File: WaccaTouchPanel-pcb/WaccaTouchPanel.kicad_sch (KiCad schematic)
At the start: 106 parts, among them IC1 W25Q16JVUXIQ_TR, IC2 AT42QT2120-MMHR, IC3 AT42QT2120-MMHR, J1 USB_C_Receptacle_USB2.0, J10 SESNSOR2, J11 SESNSOR9, J12 SESNSOR1, J13 SESNSOR10, J14 SESNSOR11, J15 SESNSOR12, J16 SESNSOR19, J17 SESNSOR18, J18 SESNSOR17, J19 SESNSOR16, J2 RJ45_LED_Shielded, J20 SESNSOR15, J21 SESNSOR20, J22 SESNSOR14, J23 SESNSOR13, J24 Conn_02x06_Odd_Even, J25 Conn_02x06_Odd_Even, J26 Conn_02x06_Odd_Even, J27 Conn_02x06_Odd_Even, J28 Conn_02x06_Odd_Even, J3 SESNSOR7, J4 SESNSOR6, J5 Conn_01x03_Male, J6 SESNSOR5, J7 SESNSOR4, J8 SESNSOR3, J9 SESNSOR8, SW1 Program, SW3 Reset, U1 NCP1117-3.3_SOT223, U3 RP2040, Y1 ABLS-12.000MHZ-B4-T

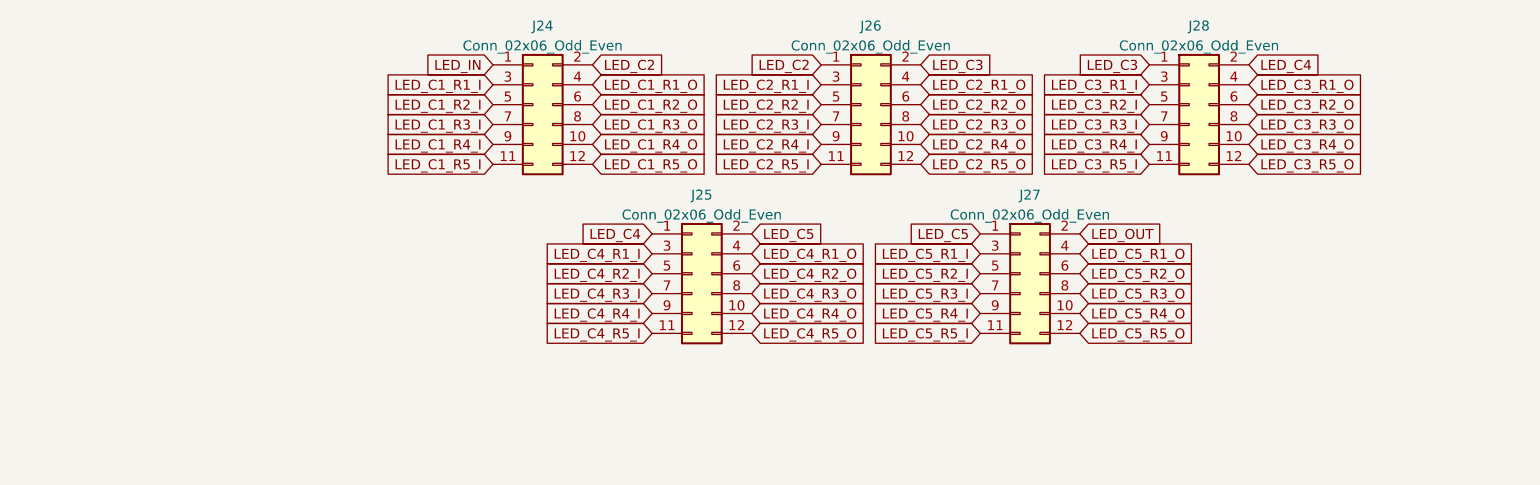
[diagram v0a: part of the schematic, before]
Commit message: finished Touch Panel PCB and added it to actions
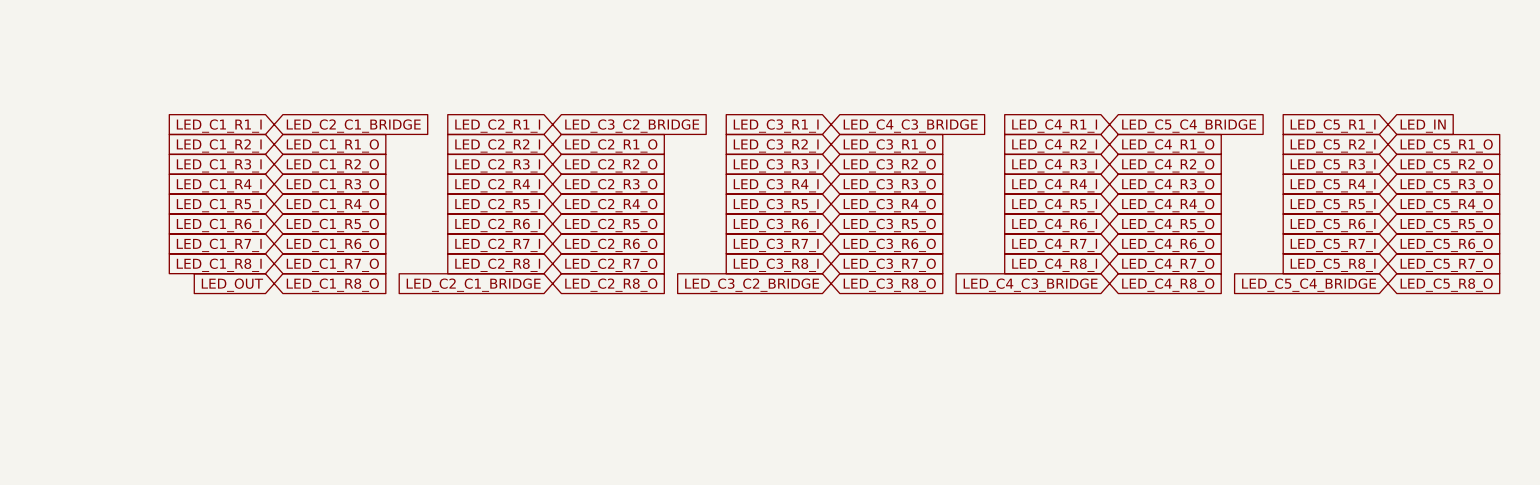
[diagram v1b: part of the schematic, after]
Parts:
- removed J24, J25, J26, J27, J28: Conn_02x06_Odd_Even, Connector_PinHeader_2.54mm:PinHeader_2x06_P2.54mm_Vertical, symbol Connector_Generic:Conn_02x06_Odd_Even
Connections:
- net LED_C1_R2_I is gone; now on net LED_C1_R1_O: D4.4 (DIN)
- net LED_C1_R3_I is gone; now on net LED_C1_R2_O: D5.4 (DIN)
- net LED_C1_R4_I is gone; now on net LED_C1_R3_O: D6.4 (DIN)
- net LED_C1_R5_I is gone; now on net LED_C1_R4_O: D7.4 (DIN)
- net LED_C1_R6_I is gone; now on net LED_C1_R5_O: D28.4 (DIN)
- net LED_C1_R7_I is gone; now on net LED_C1_R6_O: D29.4 (DIN)
- net LED_C1_R8_I is gone; now on net LED_C1_R7_O: D30.4 (DIN)
- net LED_C2_R2_I is gone; now on net LED_C2_R1_O: D9.4 (DIN)
- net LED_C2_R3_I is gone; now on net LED_C2_R2_O: D10.4 (DIN)
- net LED_C2_R4_I is gone; now on net LED_C2_R3_O: D11.4 (DIN)
- net LED_C2_R5_I is gone; now on net LED_C2_R4_O: D12.4 (DIN)
- net LED_C2_R6_I is gone; now on net LED_C2_R5_O: D31.4 (DIN)
- net LED_C2_R7_I is gone; now on net LED_C2_R6_O: D32.4 (DIN)
- net LED_C2_R8_I is gone; now on net LED_C2_R7_O: D33.4 (DIN)
- net LED_C2_R8_O is gone; now on net LED_C1_R1_I: D33.2 (DOUT)
- net LED_C3_R2_I is gone; now on net LED_C3_R1_O: D14.4 (DIN)
- net LED_C3_R3_I is gone; now on net LED_C3_R2_O: D15.4 (DIN)
- net LED_C3_R4_I is gone; now on net LED_C3_R3_O: D16.4 (DIN)
- net LED_C3_R5_I is gone; now on net LED_C3_R4_O: D17.4 (DIN)
- net LED_C3_R6_I is gone; now on net LED_C3_R5_O: D34.4 (DIN)
- net LED_C3_R7_I is gone; now on net LED_C3_R6_O: D35.4 (DIN)
- net LED_C3_R8_I is gone; now on net LED_C3_R7_O: D36.4 (DIN)
- net LED_C3_R8_O is gone; now on net LED_C2_R1_I: D36.2 (DOUT)
- net LED_C4_R2_I is gone; now on net LED_C4_R1_O: D19.4 (DIN)
- net LED_C4_R3_I is gone; now on net LED_C4_R2_O: D20.4 (DIN)
- net LED_C4_R4_I is gone; now on net LED_C4_R3_O: D21.4 (DIN)
- net LED_C4_R5_I is gone; now on net LED_C4_R4_O: D22.4 (DIN)
- net LED_C4_R6_I is gone; now on net LED_C4_R5_O: D37.4 (DIN)
- net LED_C4_R7_I is gone; now on net LED_C4_R6_O: D38.4 (DIN)
- net LED_C4_R8_I is gone; now on net LED_C4_R7_O: D39.4 (DIN)
- net LED_C4_R8_O is gone; now on net LED_C3_R1_I: D39.2 (DOUT)
- net LED_C5_R2_I is gone; now on net LED_C5_R1_O: D24.4 (DIN)
- net LED_C5_R3_I is gone; now on net LED_C5_R2_O: D25.4 (DIN)
- net LED_C5_R4_I is gone; now on net LED_C5_R3_O: D26.4 (DIN)
- net LED_C5_R5_I is gone; now on net LED_C5_R4_O: D27.4 (DIN)
- net LED_C5_R6_I is gone; now on net LED_C5_R5_O: D40.4 (DIN)
- net LED_C5_R7_I is gone; now on net LED_C5_R6_O: D41.4 (DIN)
- net LED_C5_R8_I is gone; now on net LED_C5_R7_O: D42.4 (DIN)
- net LED_C5_R8_O is gone; now on net LED_C4_R1_I: D42.2 (DOUT)
- net LED_IN is gone; now on net LED_C5_R1_I: J2.4
- net LED_OUT is gone; now on net LED_C1_R8_O: J2.2
